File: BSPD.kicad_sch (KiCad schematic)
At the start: 20 parts, among them J1 Conn_01x03, J2 Conn_01x03, J3 Conn_01x03, K0 MCCMA51-S-DC12V-C, K1 MCCMA51-S-DC12V-C, Q1 IRLZ44Z, U1 4011, U2 4011, X1 ASZKDV-32.768KHz

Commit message: Update Relay symbol
Signed-off-by: Oliver Gaskell <og305@cam.ac.uk>
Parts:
- removed K0: MCCMA51-S-DC12V-C, Additional Footprints:MCCMA51-S-DC12V-C, symbol Additional_Components:Relay
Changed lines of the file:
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@@
-	)
-	(symbol
-		(lib_id "Additional_Components:Relay")
-		(at 194.31 49.53 270)
-		(unit 1)
-		(exclude_from_sim no)
-		(in_bom yes)
-		(on_board no)
-		(dnp yes)
-		(property "Reference" "K0"
-			(at 201.4808 44.4585 90)
-			(effects
-				(font
-					(size 1.27 1.27)
-				)
-			)
-		)
-		(property "Value" "MCCMA51-S-DC12V-C"
-			(at 205.74 54.61 90)
-			(effects
-				(font
-					(size 1.27 1.27)
-				)
-			)
-		)
-		(property "Footprint" "Additional Footprints:MCCMA51-S-DC12V-C"
-			(at 194.31 49.53 0)
-			(effects
-				(font
-					(size 1.27 1.27)
-				)
-				(hide yes)
-			)
-		)
-		(property "Datasheet" "https://www.farnell.com/datasheets/3169904.pdf"
-			(at 194.31 49.53 0)
-			(effects
-				(font
-					(size 1.27 1.27)
-				)
-				(hide yes)
-			)
-		)
-		(property "Description" ""
-			(at 194.31 49.53 0)
-			(effects
-				(font
-					(size 1.27 1.27)
-				)
-				(hide yes)
-			)
-		)
-		(pin "1"
-		)
-		(pin "2"
-		)
-		(pin "3"
-		)
-		(pin "4"
-		)
-		(pin "5"
-		)
-		(instances
-			(project "New BSPD"
-				(path "/1f7c501a-057f-4634-92ce-528b01503799"
-					(reference "K0")
-					(unit 1)
-				)
-			)
-			(project "BSPD - FSG"
-				(path "/ea40ab7b-80c4-4cf6-acf9-83a05b0cd5a6"
-					(reference "K?")
-					(unit 1)
-				)
-			)
-		)
 	)
 	(symbol

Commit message: Complete new version
Signed-off-by: Oliver Gaskell <og305@cam.ac.uk>
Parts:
- removed J1, J2, J3: Conn_01x03, BSPD_footprints:ATF13-3P-BM03, symbol Connector_Generic:Conn_01x03
- added J1: Conn_01x14, FBR_Footprints:TE_776267-1, symbol Connector_Generic:Conn_01x14
- added TP5: TestPoint, TestPoint:TestPoint_Pad_D2.0mm, symbol Connector:TestPoint
- D8: footprint LED_THT:LED_D5.0mm -> LED_SMD:LED_0603_1608Metric_Pad1.05x0.95mm_HandSolder
- R1, R2: value 5K -> 100K; footprint Resistor_THT:R_Axial_DIN0207_L6.3mm_D2.5mm_P7.62mm_Horizontal -> Resistor_SMD:R_0603_1608Metric_Pad0.98x0.95mm_HandSolder
- R11: value 220R -> 180; footprint Resistor_THT:R_Axial_DIN0207_L6.3mm_D2.5mm_P7.62mm_Horizontal -> Resistor_SMD:R_0603_1608Metric_Pad0.98x0.95mm_HandSolder
- R3: footprint Resistor_THT:R_Axial_DIN0207_L6.3mm_D2.5mm_P7.62mm_Horizontal -> Resistor_SMD:R_0603_1608Metric_Pad0.98x0.95mm_HandSolder
- TP1, TP2: footprint TestPoint:TestPoint_THTPad_D3.0mm_Drill1.5mm -> TestPoint:TestPoint_Pad_D2.0mm
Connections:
- net +12V: now also J1.1 (Pin_1)
- net BPS_Power: now also J1.2 (Pin_2)
- net BPS_Sig: now also J1.3 (Pin_3)
- net CLK: now also TP5.1
- net GND: now also J1.13 (Pin_13), J1.14 (Pin_14), J1.4 (Pin_4), J1.5 (Pin_5), J1.8 (Pin_8), J1.9 (Pin_9)
- net ShutdownC: now also J1.10 (Pin_10)
- net ShutdownNC: now also J1.11 (Pin_11)
- net ShutdownNO: now also J1.12 (Pin_12)
- net TPS_Power: now also J1.6 (Pin_6)
- net TPS_Sig: now also J1.7 (Pin_7)
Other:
- note removed: "NO NC C"
- moved on the sheet: R1, R2, TP1, TP2

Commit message: Misc improvements and changes.
- Updated some silkscreen
- Added 2 more mounting holes, changed them to pads
- Updated FBR Logo
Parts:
- added H1, H2, H3, H4: MountingHole_Pad, MountingHole:MountingHole_3.2mm_M3_Pad_Via, symbol Mechanical:MountingHole_Pad
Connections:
- net GND: now also H1.1, H2.1, H3.1, H4.1

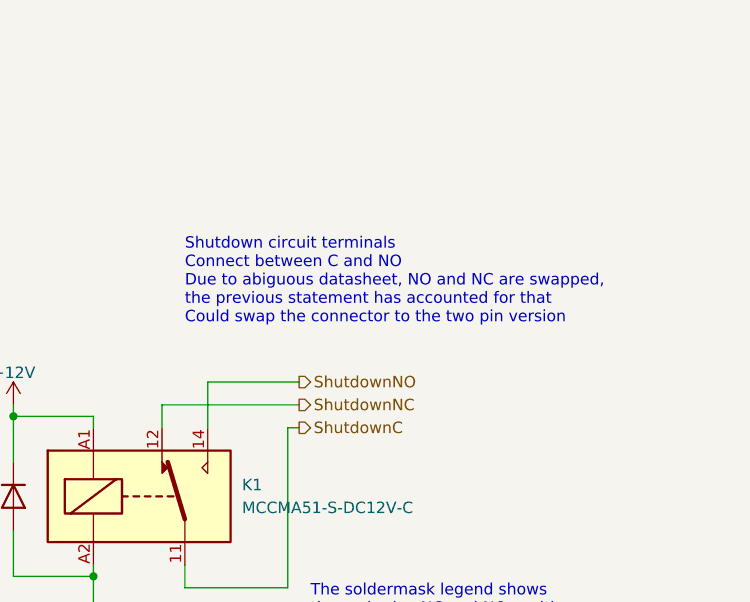
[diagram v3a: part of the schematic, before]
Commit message: Small changes, post design review
- Moving tracks away from PCB edge
- Added jumper, can be used to short shutdown
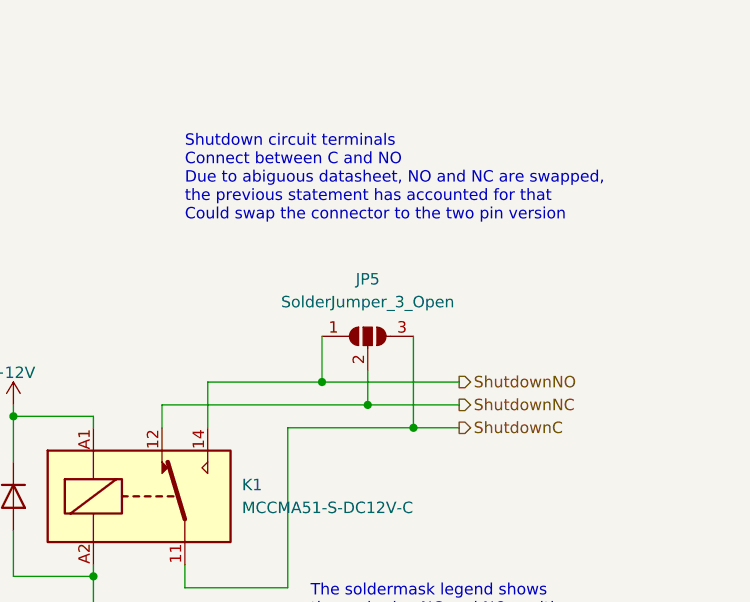
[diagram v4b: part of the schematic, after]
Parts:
- added JP5: SolderJumper_3_Open, Jumper:SolderJumper-3_P1.3mm_Open_RoundedPad1.0x1.5mm, symbol Jumper:SolderJumper_3_Open
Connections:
- net ShutdownC: now also JP5.3 (B)
- net ShutdownNC: now also JP5.2 (C)
- net ShutdownNO: now also JP5.1 (A)
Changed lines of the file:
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@@
 	(paper "A4")
+	(junction
+		(at 248.92 63.5)
+		(diameter 0)
+		(color 0 0 0 0)
+	)
+	(junction
+		(at 254 66.04)
+		(diameter 0)
+		(color 0 0 0 0)
+	)
 	(junction
 		(at 99.06 38.1)
@@
 	)
 	(junction
+		(at 243.84 60.96)
+		(diameter 0)
+		(color 0 0 0 0)
+	)
+	(junction
 		(at 152.4 156.21)
 		(diameter 0)
@@
 	(wire
 		(pts
+			(xy 248.92 63.5) (xy 259.08 63.5)
+		)
+		(stroke
+			(width 0)
+			(type default)
+		)
+	)
+	(wire
+		(pts
 			(xy 139.7 44.45) (xy 156.21 44.45)
 		)
@@
 	(wire
 		(pts
+			(xy 243.84 60.96) (xy 259.08 60.96)
+		)
+		(stroke
+			(width 0)
+			(type default)
+		)
+	)
+	(wire
+		(pts
 			(xy 162.56 156.21) (xy 162.56 154.94)
 		)
@@
 	(wire
 		(pts
-			(xy 231.14 60.96) (xy 241.3 60.96)
+			(xy 231.14 60.96) (xy 243.84 60.96)
 		)
 		(stroke
@@
 	(wire
 		(pts
+			(xy 254 55.88) (xy 254 66.04)
+		)
+		(stroke
+			(width 0)
+			(type default)
+		)
+	)
+	(wire
+		(pts
 			(xy 82.55 25.4) (xy 82.55 26.67)
 		)
@@
 	(wire
 		(pts
+			(xy 243.84 55.88) (xy 243.84 60.96)
+		)
+		(stroke
+			(width 0)
+			(type default)
+		)
+	)
+	(wire
+		(pts
 			(xy 73.66 149.86) (xy 90.17 149.86)
 		)
@@
 	(wire
 		(pts
+			(xy 248.92 59.69) (xy 248.92 63.5)
+		)
+		(stroke
+			(width 0)
+			(type default)
+		)
+	)
+	(wire
+		(pts
 			(xy 251.46 125.73) (xy 251.46 128.27)
 		)
@@
 	(wire
 		(pts
+			(xy 254 66.04) (xy 240.03 66.04)
+		)
+		(stroke
+			(width 0)
+			(type default)
+		)
+	)
+	(wire
+		(pts
 			(xy 154.94 156.21) (xy 157.48 156.21)
 		)
@@
 	(wire
 		(pts
-			(xy 241.3 66.04) (xy 240.03 66.04)
+			(xy 259.08 66.04) (xy 254 66.04)
 		)
 		(stroke
@@
 	(wire
 		(pts
-			(xy 226.06 63.5) (xy 241.3 63.5)
+			(xy 226.06 63.5) (xy 248.92 63.5)
 		)
 		(stroke
@@
 	(text "Shutdown circuit terminals\nConnect between C and NO\nDue to abiguous datasheet, NO and NC are swapped,\nthe previous statement has accounted for that\nCould swap the connector to the two pin version"
 		(exclude_from_sim no)
-		(at 228.6 54.61 0)
+		(at 228.6 43.18 0)
 		(effects
 			(font
@@
 	(hierarchical_label "ShutdownNO"
 		(shape output)
-		(at 241.3 60.96 0)
+		(at 259.08 60.96 0)
 		(fields_autoplaced yes)
 		(effects
@@
 	(hierarchical_label "ShutdownNC"
 		(shape output)
-		(at 241.3 63.5 0)
+		(at 259.08 63.5 0)
 		(fields_autoplaced yes)
 		(effects
@@
 	(hierarchical_label "ShutdownC"
 		(shape output)
-		(at 241.3 66.04 0)
+		(at 259.08 66.04 0)
 		(fields_autoplaced yes)
 		(effects
@@
 					(unit 1)
 				)
+			)
+		)
+	)
+	(symbol
+		(lib_id "Jumper:SolderJumper_3_Open")
+		(at 248.92 55.88 0)
+		(unit 1)
+		(exclude_from_sim yes)
+		(in_bom no)
+		(on_board yes)
+		(dnp no)
+		(fields_autoplaced yes)
+		(property "Reference" "JP5"
+			(at 248.92 49.53 0)
+			(effects
+				(font
+					(size 1.27 1.27)
+				)
+			)
+		)
+		(property "Value" "SolderJumper_3_Open"
+			(at 248.92 52.07 0)
+			(effects
+				(font
+					(size 1.27 1.27)
+				)
+			)
+		)
+		(property "Footprint" "Jumper:SolderJumper-3_P1.3mm_Open_RoundedPad1.0x1.5mm"
+			(at 248.92 55.88 0)
+			(effects
+				(font
+					(size 1.27 1.27)
+				)
+				(hide yes)
+			)
+		)
+		(property "Datasheet" "~"
+			(at 248.92 55.88 0)
+			(effects
+				(font
+					(size 1.27 1.27)
+				)
+				(hide yes)
+			)
+		)
+		(property "Description" "Solder Jumper, 3-pole, open"
+			(at 248.92 55.88 0)
+			(effects
+				(font
+					(size 1.27 1.27)
+				)
+				(hide yes)
+			)
+		)
+		(pin "1"
+		)
+		(pin "2"
+		)
+		(pin "3"
+		)
+		(instances
+			(project ""
+				(path "/1f7c501a-057f-4634-92ce-528b01503799"
+					(reference "JP5")
+					(unit 1)
+				)
